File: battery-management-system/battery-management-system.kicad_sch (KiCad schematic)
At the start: 0 parts

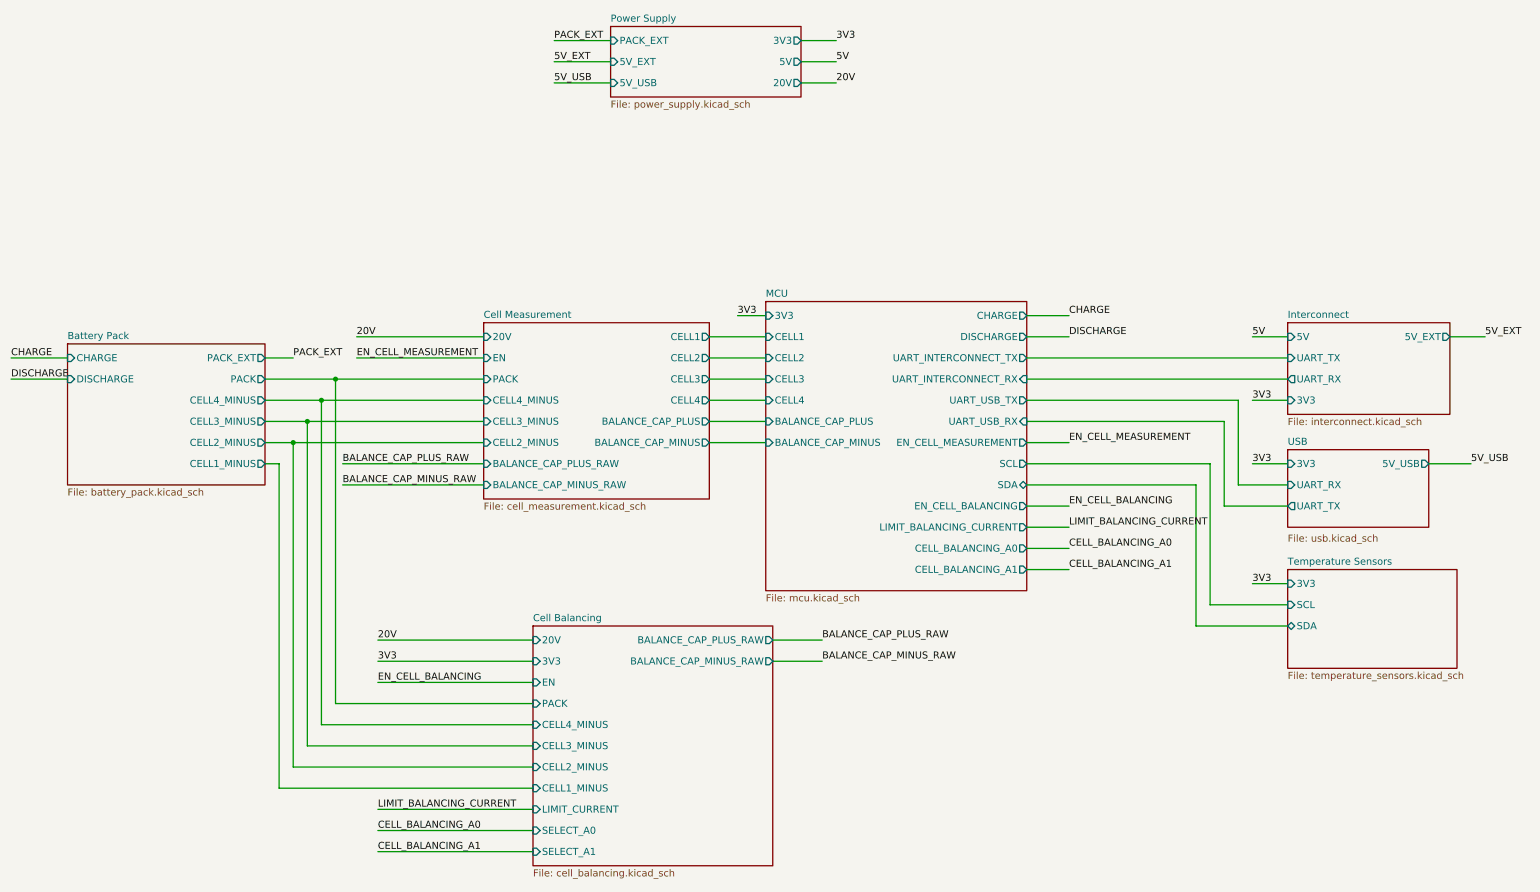
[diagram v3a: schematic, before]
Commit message: implement balancing
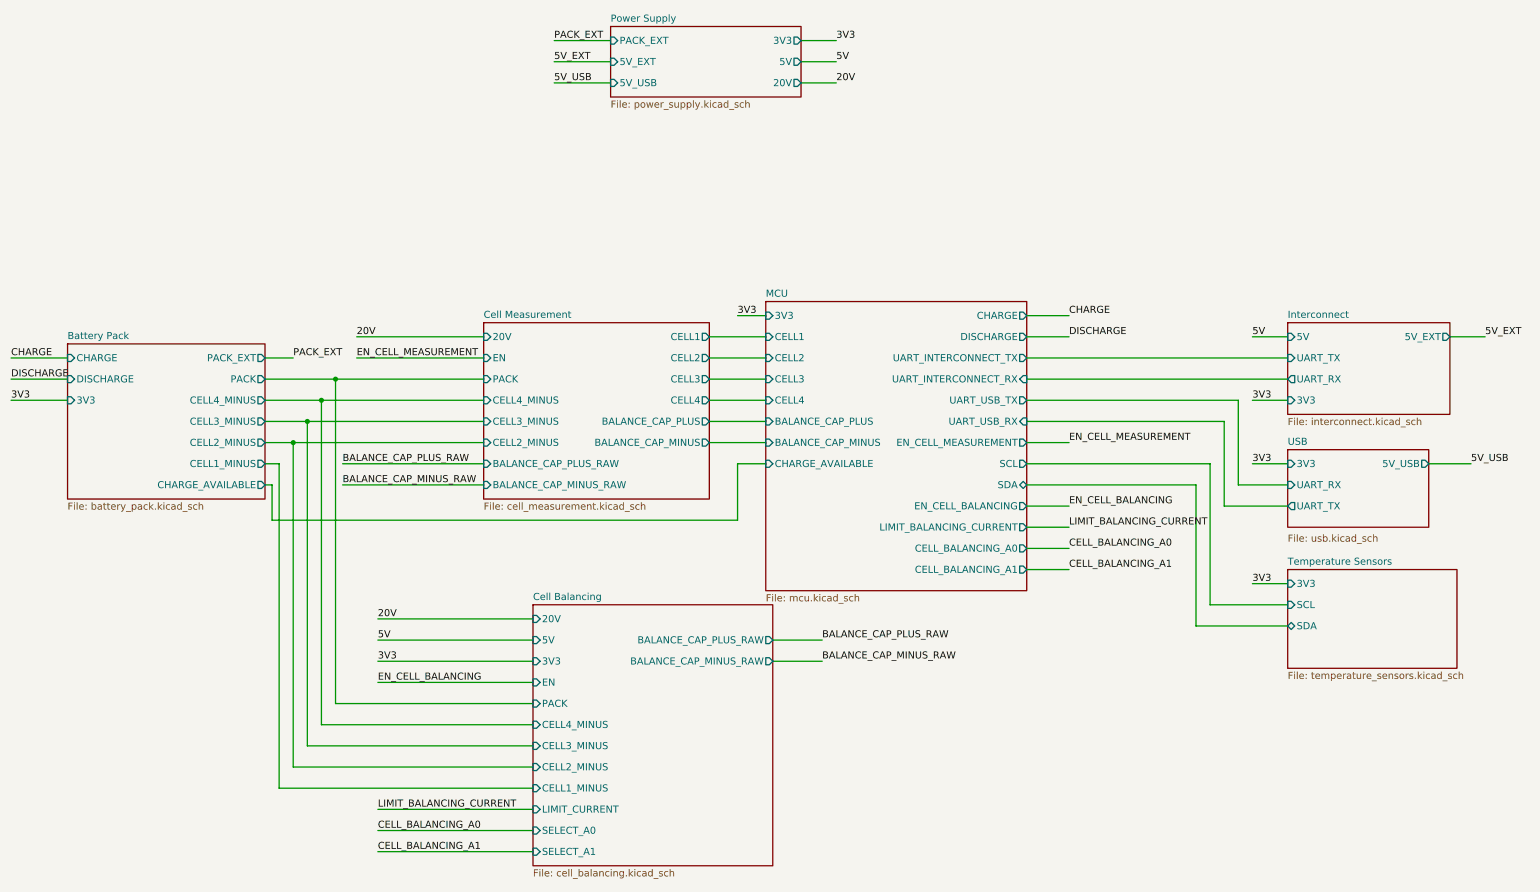
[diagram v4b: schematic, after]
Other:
- sheet Battery Pack ports: added 3V3, CHARGE_AVAILABLE; removed none
- sheet Cell Balancing ports: added 5V; removed none
- sheet MCU ports: added CHARGE_AVAILABLE; removed none
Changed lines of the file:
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@@
+    (stroke (width 0) (type default))
+  )
+  (wire (pts (xy 143.51 113.03) (xy 59.69 113.03))
+    (stroke (width 0) (type default))
+  )
+  (wire (pts (xy 12.7 91.44) (xy 22.86 91.44))
     (stroke (width 0) (type default))
   )
@@
     (stroke (width 0) (type default))
   )
+  (wire (pts (xy 59.69 113.03) (xy 59.69 106.68))
+    (stroke (width 0) (type default))
+  )
   (wire (pts (xy 154.94 34.29) (xy 161.29 34.29))
     (stroke (width 0) (type default))
@@
     (stroke (width 0) (type default))
   )
+  (wire (pts (xy 143.51 102.87) (xy 143.51 113.03))
+    (stroke (width 0) (type default))
+  )
   (wire (pts (xy 228.6 102.87) (xy 228.6 128.27))
     (stroke (width 0) (type default))
@@
     (stroke (width 0) (type default))
   )
+  (wire (pts (xy 78.74 130.81) (xy 106.68 130.81))
+    (stroke (width 0) (type default))
+  )
   (wire (pts (xy 231.14 95.25) (xy 231.14 110.49))
     (stroke (width 0) (type default))
@@
     (stroke (width 0) (type default))
   )
+  (wire (pts (xy 59.69 106.68) (xy 58.42 106.68))
+    (stroke (width 0) (type default))
+  )
   (wire (pts (xy 271.78 80.01) (xy 278.13 80.01))
     (stroke (width 0) (type default))
@@
     (stroke (width 0) (type default))
   )
+  (wire (pts (xy 148.59 102.87) (xy 143.51 102.87))
+    (stroke (width 0) (type default))
+  )
   (wire (pts (xy 72.39 102.87) (xy 97.79 102.87))
     (stroke (width 0) (type default))
@@
     (effects (font (size 1.27 1.27)) (justify left bottom))
   )
-  (label "20V" (at 78.74 134.62 0) (fields_autoplaced)
+  (label "20V" (at 78.74 130.81 0) (fields_autoplaced)
     (effects (font (size 1.27 1.27)) (justify left bottom))
   )
@@
     (effects (font (size 1.27 1.27)) (justify left bottom))
   )
+  (label "3V3" (at 12.7 91.44 0) (fields_autoplaced)
+    (effects (font (size 1.27 1.27)) (justify left bottom))
+  )
+  (label "5V" (at 78.74 134.62 0) (fields_autoplaced)
+    (effects (font (size 1.27 1.27)) (justify left bottom))
+  )
   (label "3V3" (at 78.74 138.43 0) (fields_autoplaced)
     (effects (font (size 1.27 1.27)) (justify left bottom))
@@
     (effects (font (size 1.27 1.27)) (justify left bottom))
   )
-  (sheet (at 22.86 81.28) (size 35.56 25.4) (fields_autoplaced)
+  (sheet (at 22.86 81.28) (size 35.56 27.94) (fields_autoplaced)
     (stroke (width 0.1524) (type solid))
     (fill (color 0 0 0 0.0000))
@@
       (effects (font (size 1.27 1.27)) (justify left bottom))
     )
-    (property "Sheetfile" "battery_pack.kicad_sch" (at 22.86 107.2646 0)
+    (property "Sheetfile" "battery_pack.kicad_sch" (at 22.86 109.8046 0)
       (effects (font (size 1.27 1.27)) (justify left top))
     )
@@
     )
     (pin "CELL1_MINUS" output (at 58.42 102.87 0)
+      (effects (font (size 1.27 1.27)) (justify right))
+    )
+    (pin "3V3" input (at 22.86 91.44 180)
+      (effects (font (size 1.27 1.27)) (justify left))
+    )
+    (pin "CHARGE_AVAILABLE" output (at 58.42 106.68 0)
       (effects (font (size 1.27 1.27)) (justify right))
     )
@@
     )
   )
-  (sheet (at 106.68 132.08) (size 43.18 43.18) (fields_autoplaced)
+  (sheet (at 106.68 128.27) (size 43.18 46.99) (fields_autoplaced)
     (stroke (width 0.1524) (type solid))
     (fill (color 0 0 0 0.0000))
-    (property "Sheetname" "Cell Balancing" (at 106.68 131.3684 0)
+    (property "Sheetname" "Cell Balancing" (at 106.68 127.5584 0)
       (effects (font (size 1.27 1.27)) (justify left bottom))
     )
@@
       (effects (font (size 1.27 1.27)) (justify left))
     )
-    (pin "20V" input (at 106.68 134.62 180)
+    (pin "20V" input (at 106.68 130.81 180)
       (effects (font (size 1.27 1.27)) (justify left))
     )
     (pin "3V3" input (at 106.68 138.43 180)
+      (effects (font (size 1.27 1.27)) (justify left))
+    )
+    (pin "5V" input (at 106.68 134.62 180)
       (effects (font (size 1.27 1.27)) (justify left))
     )
@@
       (effects (font (size 1.27 1.27)) (justify right))
     )
+    (pin "CHARGE_AVAILABLE" input (at 148.59 102.87 180)
+      (effects (font (size 1.27 1.27)) (justify left))
+    )
     (instances

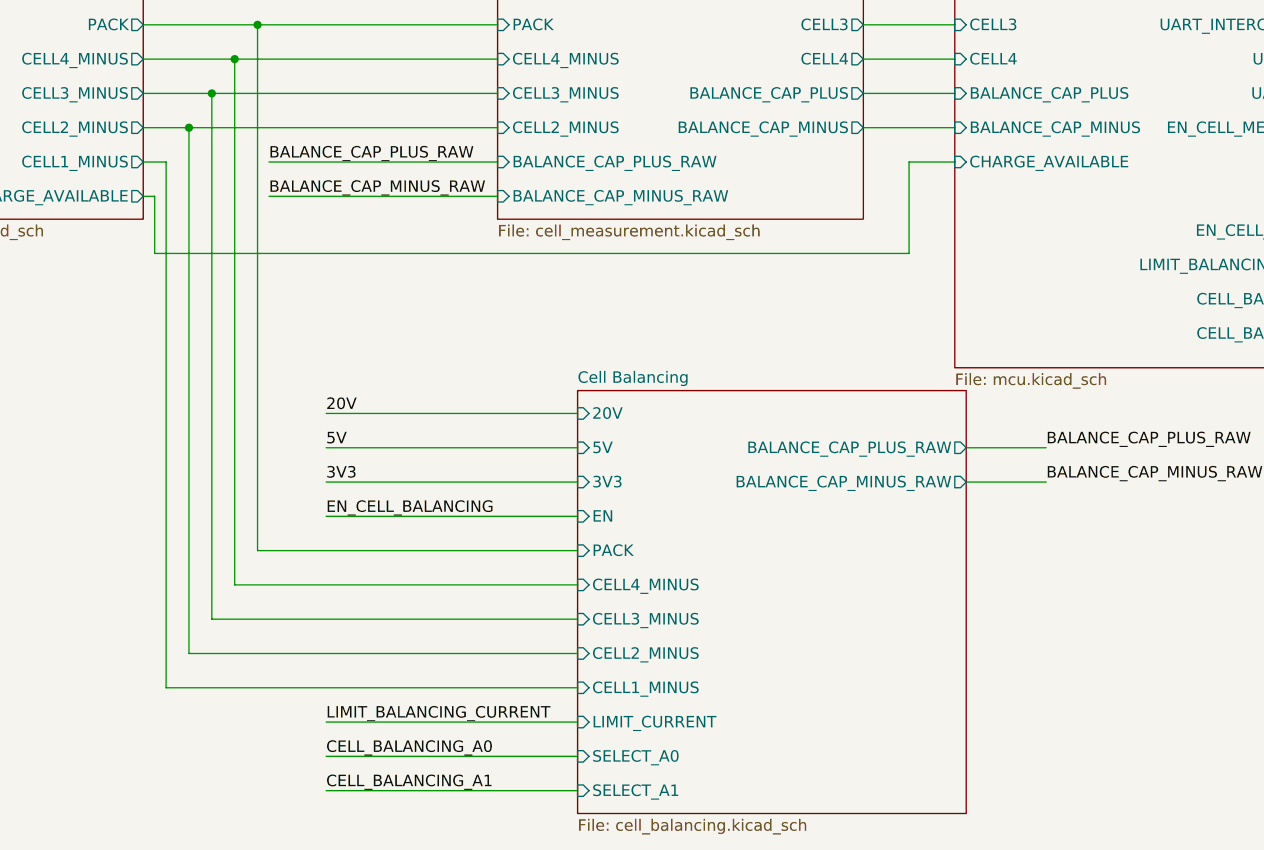
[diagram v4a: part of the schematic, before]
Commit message: add fuel gauge IC
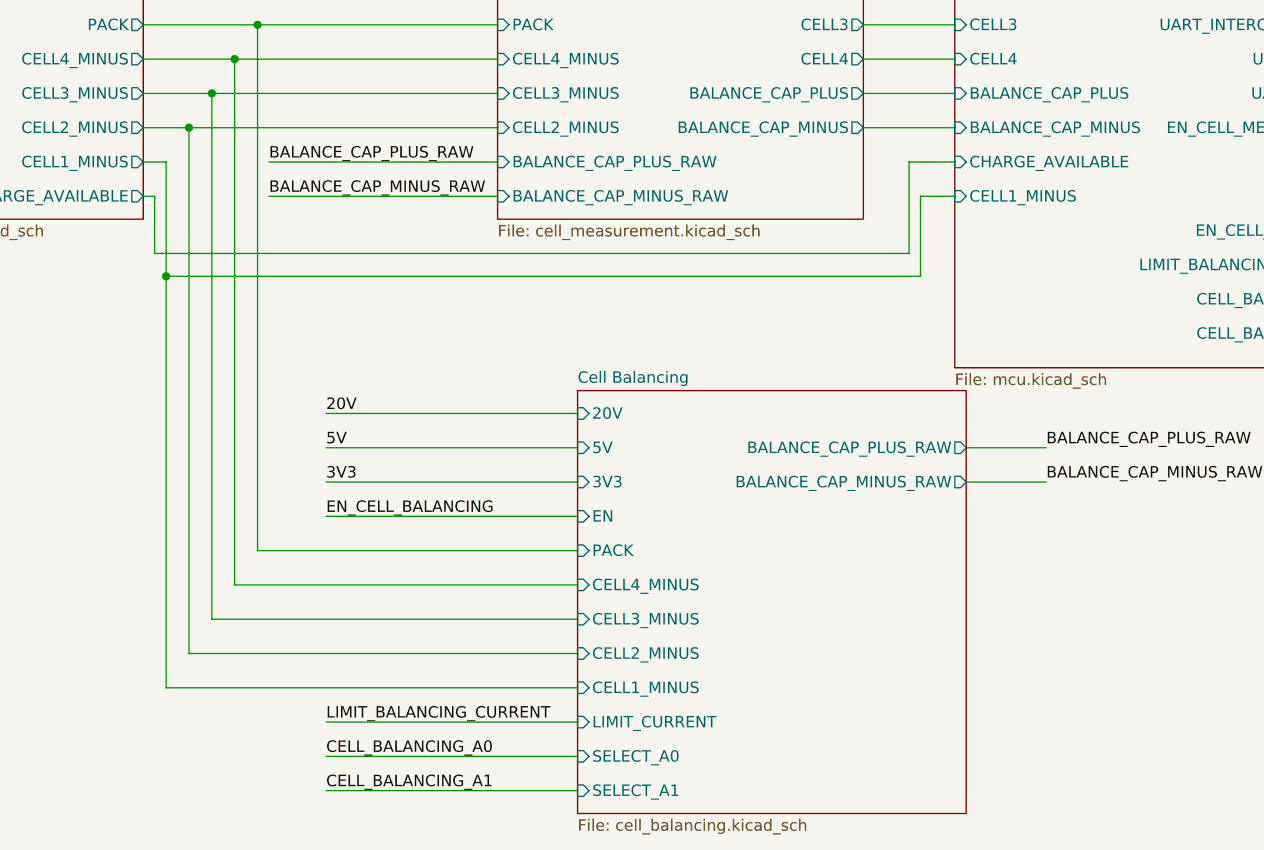
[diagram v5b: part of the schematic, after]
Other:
- sheet MCU ports: added CELL1_MINUS; removed none
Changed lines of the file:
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@@
   (junction (at 68.58 91.44) (diameter 0) (color 0 0 0 0)
   )
+  (junction (at 60.96 115.57) (diameter 0) (color 0 0 0 0)
+  )
   (wire (pts (xy 58.42 87.63) (xy 71.12 87.63))
     (stroke (width 0) (type default))
@@
     (stroke (width 0) (type default))
   )
-  (wire (pts (xy 60.96 161.29) (xy 60.96 102.87))
+  (wire (pts (xy 60.96 161.29) (xy 60.96 115.57))
     (stroke (width 0) (type default))
   )
@@
     (stroke (width 0) (type default))
   )
+  (wire (pts (xy 144.78 115.57) (xy 60.96 115.57))
+    (stroke (width 0) (type default))
+  )
   (wire (pts (xy 226.06 132.08) (xy 242.57 132.08))
     (stroke (width 0) (type default))
@@
     (stroke (width 0) (type default))
   )
+  (wire (pts (xy 60.96 115.57) (xy 60.96 102.87))
+    (stroke (width 0) (type default))
+  )
+  (wire (pts (xy 144.78 106.68) (xy 144.78 115.57))
+    (stroke (width 0) (type default))
+  )
   (wire (pts (xy 110.49 30.48) (xy 120.65 30.48))
     (stroke (width 0) (type default))
@@
   )
   (wire (pts (xy 195.58 80.01) (xy 203.2 80.01))
+    (stroke (width 0) (type default))
+  )
+  (wire (pts (xy 144.78 106.68) (xy 148.59 106.68))
     (stroke (width 0) (type default))
   )
@@
       (effects (font (size 1.27 1.27)) (justify left))
     )
+    (pin "CELL1_MINUS" input (at 148.59 106.68 180)
+      (effects (font (size 1.27 1.27)) (justify left))
+    )

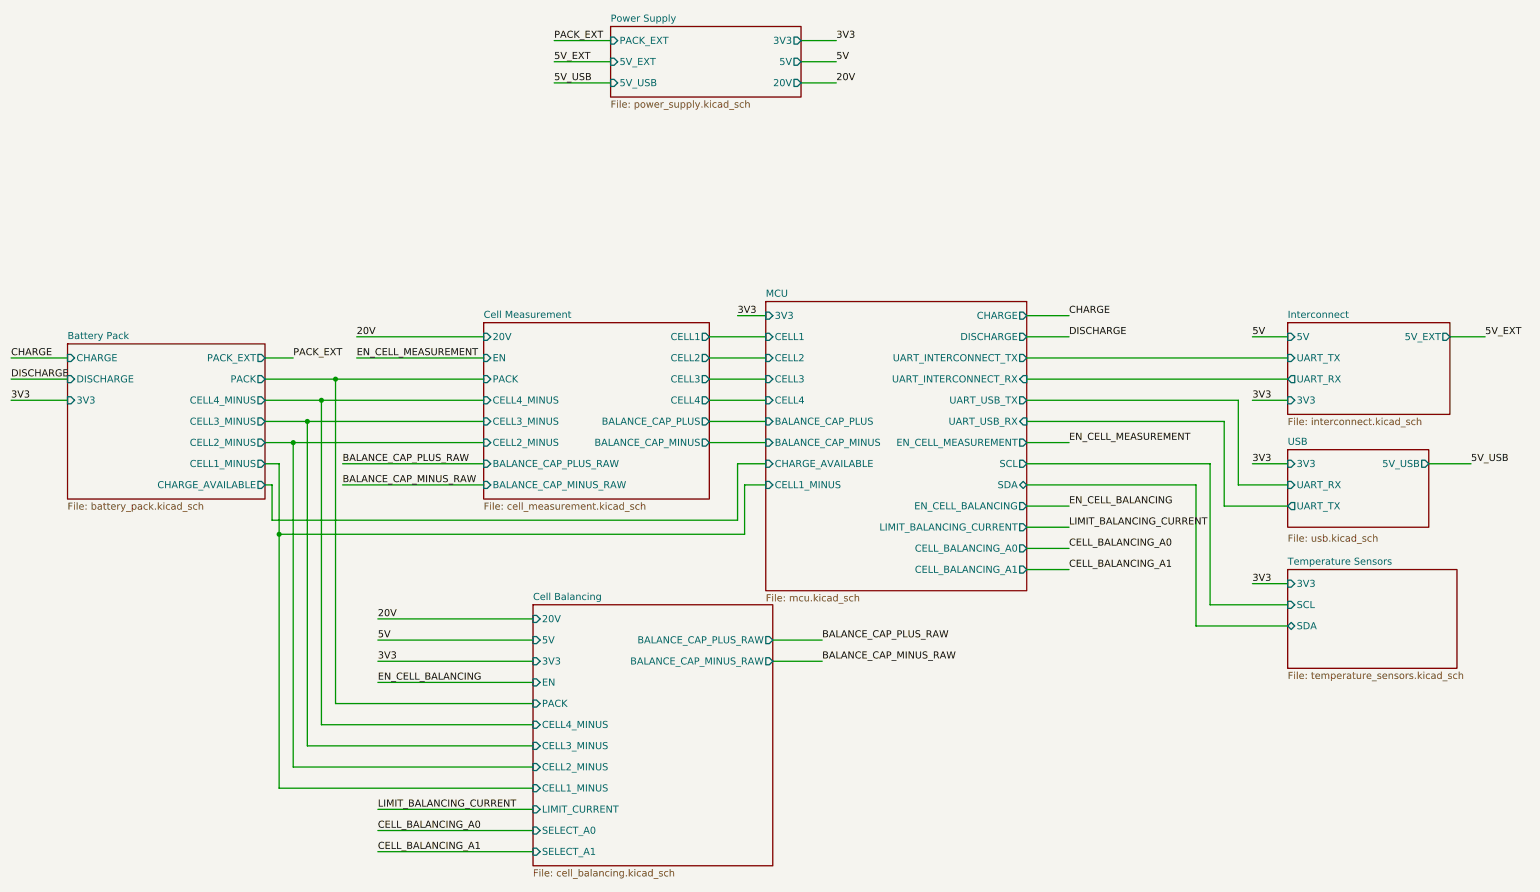
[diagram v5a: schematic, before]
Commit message: fix current sensing
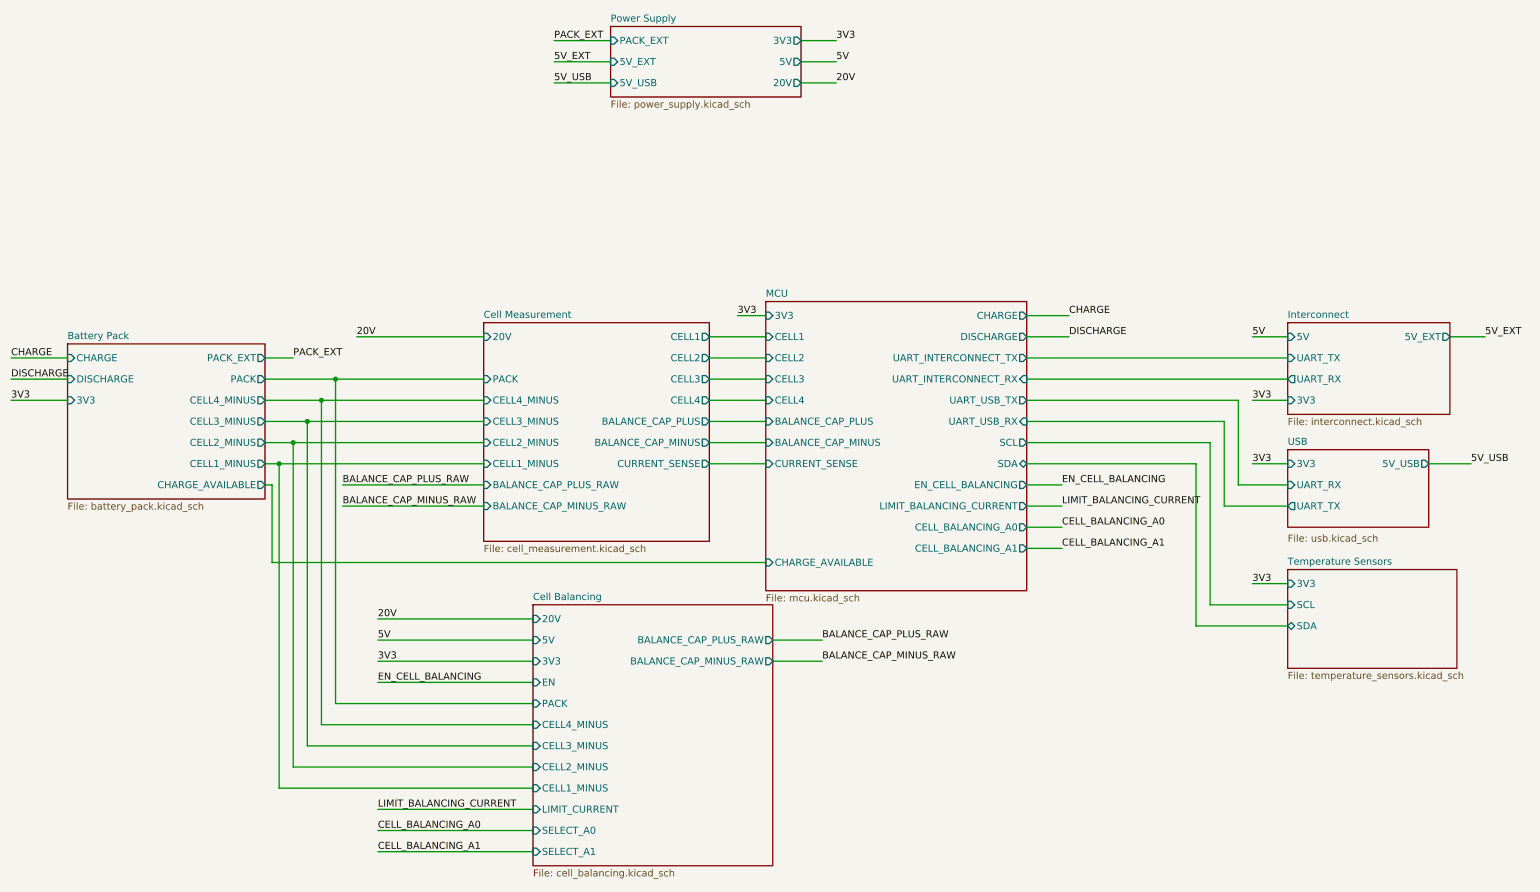
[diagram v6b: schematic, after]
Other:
- sheet Cell Measurement ports: added CELL1_MINUS, CURRENT_SENSE; removed EN
- sheet MCU ports: added CURRENT_SENSE; removed CELL1_MINUS, EN_CELL_MEASUREMENT
